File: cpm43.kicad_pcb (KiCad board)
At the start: 2 copper layers, 232.2 x 76.7 mm, 186 parts, among them J1 Conn_01x04, Q1 Q_NPN_BCE, SW1 SW_PUSH, U1 ATmega32U4, U2 PRTR5V0U2X, X1 Crystal_GND24

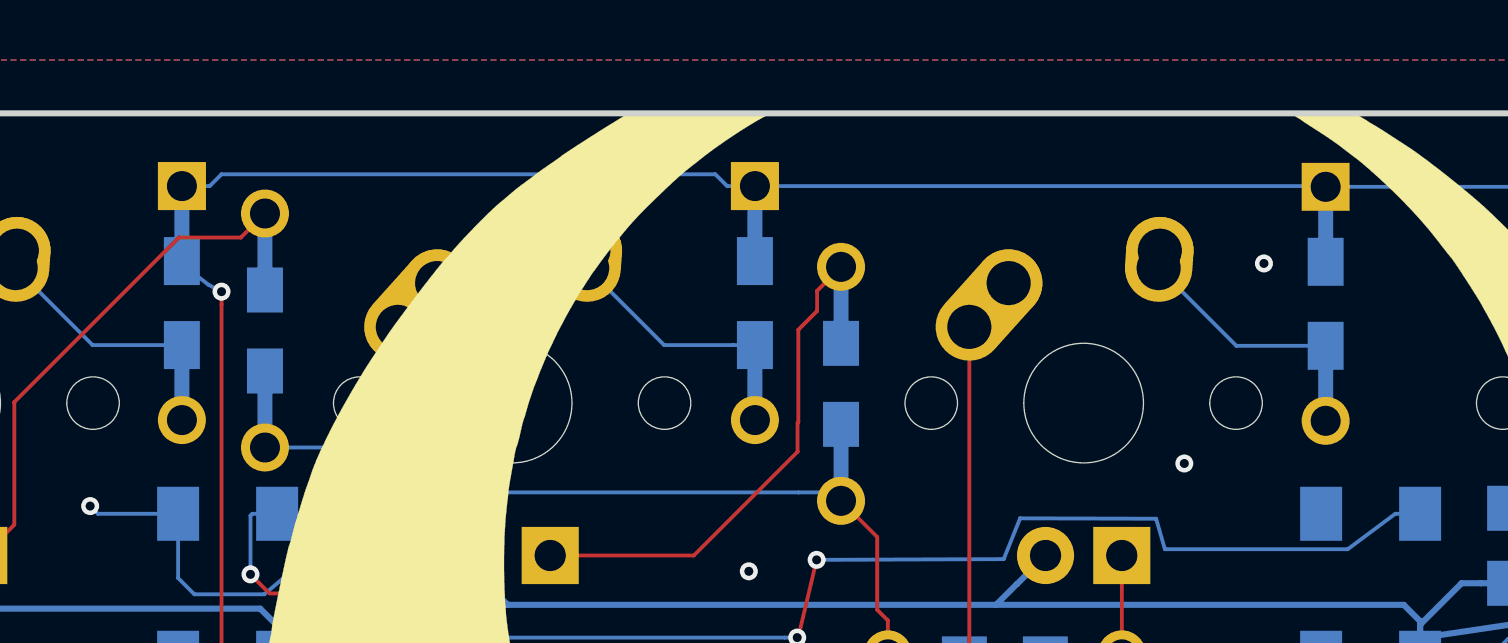
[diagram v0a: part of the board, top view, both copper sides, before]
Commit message: Mounting holes added
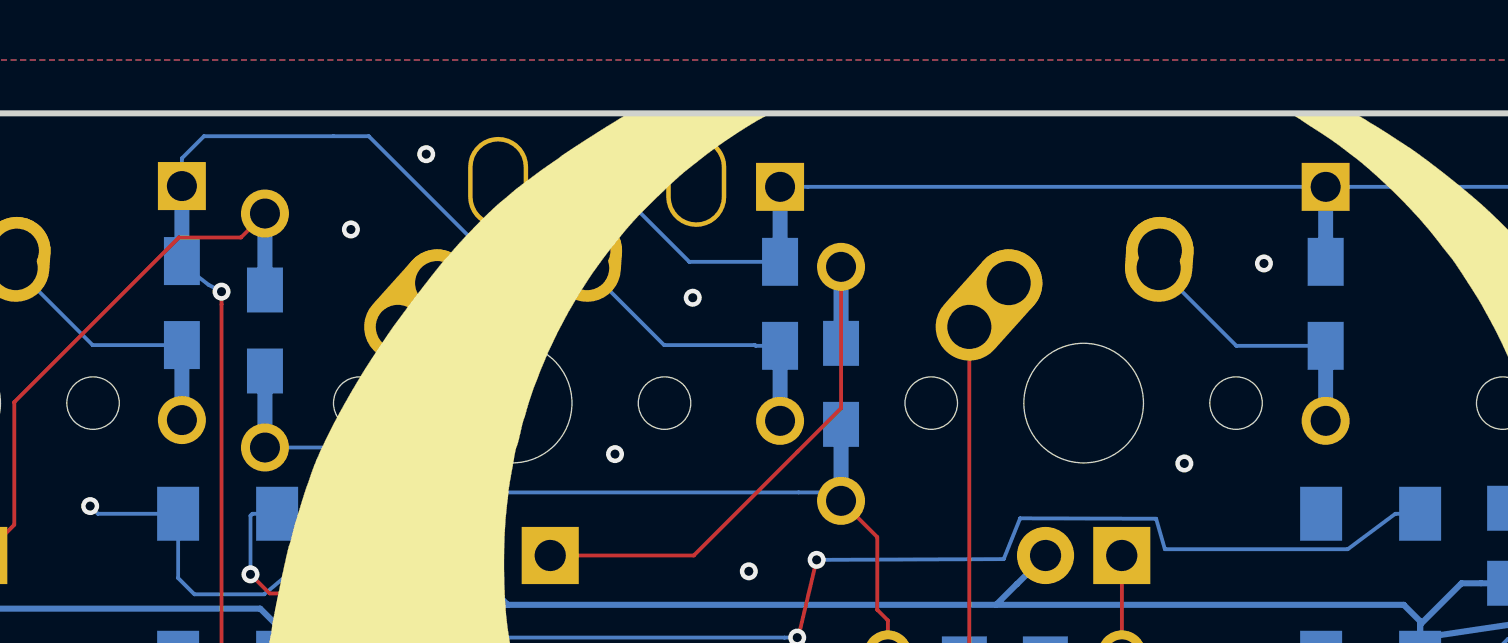
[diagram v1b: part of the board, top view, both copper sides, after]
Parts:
- added P?: CONN_1, keyboard_parts:PIN_1, F.Cu at (68.7, 62.5)
- added P?: CONN_1, keyboard_parts:PIN_1, F.Cu at (62.1, 62.5)
- moved D2 0.84 mm to (71.5, 66.5)
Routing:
- net ROW0: track 323.4 -> 327.5 mm
- net Net-(D2-Pad2): track 7.18 -> 8.07 mm
- net GND: vias 170 -> 175
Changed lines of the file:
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@@
     (thickness 1.6)
     (drawings 53)
-    (tracks 2463)
+    (tracks 2472)
     (zones 0)
-    (modules 186)
+    (modules 188)
     (nets 139)
   )
@@
     (38 B.Mask user)
     (39 F.Mask user)
-    (40 Dwgs.User user hide)
+    (40 Dwgs.User user)
     (41 Cmts.User user hide)
     (42 Eco1.User user hide)
@@
     (mod_text_size 1 1)
     (mod_text_width 0.15)
-    (pad_size 1.5 1.5)
-    (pad_drill 0.6)
+    (pad_size 3 2)
+    (pad_drill 2.7)
     (pad_to_mask_clearance 0)
     (aux_axis_origin 0 0)
@@
     (add_net VCC)
   )
+  (module keyboard_parts:PIN_1 (layer F.Cu)
+    (at 68.707 62.484 90)
+    (tags "CONN pin 1 circle")
+    (fp_text reference P? (at 0 -1.45 90) (layer F.SilkS) hide
+      (effects (font (size 0.8 0.8) (thickness 0.15)))
+    )
+    (fp_text value CONN_1 (at 0 -1.45 90) (layer F.SilkS) hide
+      (effects (font (size 0.8 0.8) (thickness 0.15)))
+    )
+    (pad 1 thru_hole oval (at 0 0 90) (size 3 2) (drill oval 2.7 1.7) (layers *.Cu *.Mask))
+  )
   (module Buttons_Switches_SMD:SW_SPST_TL3342 (layer B.Cu)
     (at 233.3244 85.852 270)
@@
   )
   (module Keebio-Parts:Diode-Hybrid-Back (layer F.Cu)
-    (at 70.6628 66.5226 90)
+    (at 71.501 66.548 90)
     (attr smd)
     (fp_text reference D2 (at 0.1016 -1.4478 90) (layer B.SilkS)
@@
     (pad 1 thru_hole rect (at 0 0 270) (size 1.7 1.7) (drill 1) (layers *.Cu *.Mask)
       (net 2 GND))
-    (model ${KISYS3DMOD}/Pin_Headers.3dshapes/Pin_Header_Straight_1x04_Pitch2.54mm.wrl
-      (at (xyz 0 0 0))
-      (scale (xyz 1 1 1))
-      (rotate (xyz 0 0 0))
+  )
+  (module keyboard_parts:PIN_1 (layer F.Cu)
+    (at 62.103 62.484 90)
+    (tags "CONN pin 1 circle")
+    (fp_text reference P? (at 0 -1.45 90) (layer F.SilkS) hide
+      (effects (font (size 0.8 0.8) (thickness 0.15)))
     )
+    (fp_text value CONN_1 (at 0 -1.45 90) (layer F.SilkS) hide
+      (effects (font (size 0.8 0.8) (thickness 0.15)))
+    )
+    (pad 1 thru_hole oval (at 0 0 90) (size 3 2) (drill oval 2.7 1.7) (layers *.Cu *.Mask))
   )
   (gr_text GND (at 59.8678 79.8322 90) (layer B.SilkS)
@@
   (via (at 60.1472 85.598) (size 0.6) (drill 0.3) (layers F.Cu B.Cu) (net 2))
   (via (at 80.7974 83.566) (size 0.6) (drill 0.3) (layers F.Cu B.Cu) (net 2))
+  (via (at 57.19572 64.06896) (size 0.6) (drill 0.3) (layers F.Cu B.Cu) (net 2))
+  (via (at 65.99936 71.55688) (size 0.6) (drill 0.3) (layers F.Cu B.Cu) (net 2))
+  (via (at 68.59016 66.3448) (size 0.6) (drill 0.3) (layers F.Cu B.Cu) (net 2))
+  (via (at 65.28816 61.8744) (size 0.6) (drill 0.3) (layers F.Cu B.Cu) (net 2))
+  (via (at 59.70524 61.55944) (size 0.6) (drill 0.3) (layers F.Cu B.Cu) (net 2))
   (segment (start 109.093 118.257) (end 109.875 117.475) (width 0.127) (layer B.Cu) (net 3))
   (segment (start 109.093 120.523) (end 109.093 118.257) (width 0.127) (layer B.Cu) (net 3))
@@
   (segment (start 48.58608 67.9226) (end 51.562 67.9226) (width 0.127) (layer B.Cu) (net 5))
   (segment (start 46.01996 65.35648) (end 48.58608 67.9226) (width 0.127) (layer B.Cu) (net 5))
-  (segment (start 52.489 62.6226) (end 52.8816 62.23) (width 0.127) (layer B.Cu) (net 6))
-  (segment (start 51.562 62.6226) (end 52.489 62.6226) (width 0.127) (layer B.Cu) (net 6))
-  (segment (start 69.7358 62.6226) (end 70.6628 62.6226) (width 0.127) (layer B.Cu) (net 6))
-  (segment (start 69.3432 62.23) (end 69.7358 62.6226) (width 0.127) (layer B.Cu) (net 6))
-  (segment (start 52.8816 62.23) (end 69.3432 62.23) (width 0.127) (layer B.Cu) (net 6))
   (segment (start 89.662 62.6226) (end 89.6874 62.648) (width 0.127) (layer B.Cu) (net 6))
-  (segment (start 70.6628 62.6226) (end 89.662 62.6226) (width 0.127) (layer B.Cu) (net 6))
   (segment (start 108.6104 62.648) (end 108.7628 62.8004) (width 0.127) (layer B.Cu) (net 6))
   (segment (start 89.6874 62.648) (end 108.6104 62.648) (width 0.127) (layer B.Cu) (net 6))
@@
   (segment (start 97.8916 120.1166) (end 110.207224 120.5103) (width 0.127) (layer F.Cu) (net 6))
   (via (at 97.8916 120.1166) (size 0.6) (drill 0.3) (layers F.Cu B.Cu) (net 6))
+  (segment (start 51.562 61.6956) (end 52.2976 60.96) (width 0.127) (layer B.Cu) (net 6))
+  (segment (start 51.562 62.6226) (end 51.562 61.6956) (width 0.127) (layer B.Cu) (net 6))
+  (segment (start 56.61152 60.96) (end 57.79008 60.96) (width 0.127) (layer B.Cu) (net 6))
+  (segment (start 52.2976 60.96) (end 56.61152 60.96) (width 0.127) (layer B.Cu) (net 6))
+  (segment (start 57.79008 60.96) (end 61.7474 64.91732) (width 0.127) (layer B.Cu) (net 6))
+  (segment (start 61.7474 64.91732) (end 62.59068 64.91732) (width 0.127) (layer B.Cu) (net 6))
+  (segment (start 62.59068 64.91732) (end 64.35344 63.15456) (width 0.127) (layer B.Cu) (net 6))
+  (segment (start 64.35344 63.15456) (end 66.48196 63.15456) (width 0.127) (layer B.Cu) (net 6))
+  (segment (start 68.4754 65.148) (end 71.501 65.148) (width 0.127) (layer B.Cu) (net 6))
+  (segment (start 66.48196 63.15456) (end 68.4754 65.148) (width 0.127) (layer B.Cu) (net 6))
+  (segment (start 72.428 62.648) (end 89.6874 62.648) (width 0.127) (layer B.Cu) (net 6))
+  (segment (start 71.501 62.648) (end 72.428 62.648) (width 0.127) (layer B.Cu) (net 6))
   (segment (start 65.06996 65.35648) (end 65.59668 65.35648) (width 0.127) (layer F.Cu) (net 7))
-  (segment (start 69.9358 67.9226) (end 70.6628 67.9226) (width 0.127) (layer B.Cu) (net 7))
-  (segment (start 67.63608 67.9226) (end 69.9358 67.9226) (width 0.127) (layer B.Cu) (net 7))
-  (segment (start 65.06996 65.35648) (end 67.63608 67.9226) (width 0.127) (layer B.Cu) (net 7))
   (segment (start 84.11996 65.35648) (end 84.59588 65.35648) (width 0.127) (layer F.Cu) (net 8))
   (segment (start 86.71148 67.948) (end 89.6874 67.948) (width 0.127) (layer B.Cu) (net 8))
@@
   (segment (start 63.52052 86.36648) (end 63.52052 84.3788) (width 0.127) (layer F.Cu) (net 69))
   (segment (start 63.52052 84.3788) (end 61.468 84.3788) (width 0.127) (layer F.Cu) (net 69))
-  (segment (start 72.733001 66.114999) (end 72.733001 66.789199) (width 0.127) (layer F.Cu) (net 70))
-  (segment (start 73.533 65.315) (end 72.733001 66.114999) (width 0.127) (layer F.Cu) (net 70))
-  (segment (start 72.733001 66.789199) (end 72.1106 67.4116) (width 0.127) (layer F.Cu) (net 70))
-  (segment (start 72.1106 70.489582) (end 72.0852 70.514982) (width 0.127) (layer F.Cu) (net 70))
-  (segment (start 72.1106 67.4116) (end 72.1106 70.489582) (width 0.127) (layer F.Cu) (net 70))
-  (segment (start 72.0852 70.514982) (end 72.0852 71.4756) (width 0.127) (layer F.Cu) (net 70))
+  (segment (start 72.1106 70.489582) (end 72.0852 70.514982) (width 0.127) (layer F.Cu) (net 7))
+  (segment (start 70.6882 67.948) (end 71.501 67.948) (width 0.127) (layer B.Cu) (net 7))
+  (segment (start 70.6628 67.9226) (end 70.6882 67.948) (width 0.127) (layer B.Cu) (net 7))
+  (segment (start 65.06996 65.35648) (end 67.63608 67.9226) (width 0.127) (layer B.Cu) (net 7))
+  (segment (start 67.63608 67.9226) (end 70.6628 67.9226) (width 0.127) (layer B.Cu) (net 7))
   (segment (start 68.62432 74.93648) (end 63.83996 74.93648) (width 0.127) (layer F.Cu) (net 70))
   (segment (start 72.0852 71.4756) (end 68.62432 74.93648) (width 0.127) (layer F.Cu) (net 70))
+  (segment (start 73.533 70.0278) (end 73.533 65.315) (width 0.127) (layer F.Cu) (net 70))
+  (segment (start 72.0852 71.4756) (end 73.533 70.0278) (width 0.127) (layer F.Cu) (net 70))
   (segment (start 77.80996 78.83592) (end 83.88052 84.90648) (width 0.127) (layer F.Cu) (net 71))
   (segment (start 77.80996 67.31648) (end 77.80996 78.83592) (width 0.127) (layer F.Cu) (net 71))

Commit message: _
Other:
- board text added: "JLCJLCJLCJLC"
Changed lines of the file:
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@@
   (general
     (thickness 1.6)
-    (drawings 53)
+    (drawings 54)
     (tracks 2472)
     (zones 0)
@@
     (pad 1 thru_hole oval (at 0 0 90) (size 3 2) (drill oval 2.7 1.7) (layers *.Cu *.Mask))
   )
+  (gr_text JLCJLCJLCJLC (at 50.87112 134.86892) (layer B.SilkS)
+    (effects (font (size 0.9 0.9) (thickness 0.225)))
+  )
   (gr_text GND (at 59.8678 79.8322 90) (layer B.SilkS)
     (effects (font (size 0.8 0.8) (thickness 0.15)) (justify mirror))
@@
   (segment (start 71.501 62.648) (end 72.428 62.648) (width 0.127) (layer B.Cu) (net 6))
   (segment (start 65.06996 65.35648) (end 65.59668 65.35648) (width 0.127) (layer F.Cu) (net 7))
+  (segment (start 72.1106 70.489582) (end 72.0852 70.514982) (width 0.127) (layer F.Cu) (net 7))
+  (segment (start 70.6882 67.948) (end 71.501 67.948) (width 0.127) (layer B.Cu) (net 7))
+  (segment (start 70.6628 67.9226) (end 70.6882 67.948) (width 0.127) (layer B.Cu) (net 7))
+  (segment (start 65.06996 65.35648) (end 67.63608 67.9226) (width 0.127) (layer B.Cu) (net 7))
+  (segment (start 67.63608 67.9226) (end 70.6628 67.9226) (width 0.127) (layer B.Cu) (net 7))
   (segment (start 84.11996 65.35648) (end 84.59588 65.35648) (width 0.127) (layer F.Cu) (net 8))
   (segment (start 86.71148 67.948) (end 89.6874 67.948) (width 0.127) (layer B.Cu) (net 8))
@@
   (segment (start 63.52052 86.36648) (end 63.52052 84.3788) (width 0.127) (layer F.Cu) (net 69))
   (segment (start 63.52052 84.3788) (end 61.468 84.3788) (width 0.127) (layer F.Cu) (net 69))
-  (segment (start 72.1106 70.489582) (end 72.0852 70.514982) (width 0.127) (layer F.Cu) (net 7))
-  (segment (start 70.6882 67.948) (end 71.501 67.948) (width 0.127) (layer B.Cu) (net 7))
-  (segment (start 70.6628 67.9226) (end 70.6882 67.948) (width 0.127) (layer B.Cu) (net 7))
-  (segment (start 65.06996 65.35648) (end 67.63608 67.9226) (width 0.127) (layer B.Cu) (net 7))
-  (segment (start 67.63608 67.9226) (end 70.6628 67.9226) (width 0.127) (layer B.Cu) (net 7))
   (segment (start 68.62432 74.93648) (end 63.83996 74.93648) (width 0.127) (layer F.Cu) (net 70))
   (segment (start 72.0852 71.4756) (end 68.62432 74.93648) (width 0.127) (layer F.Cu) (net 70))
